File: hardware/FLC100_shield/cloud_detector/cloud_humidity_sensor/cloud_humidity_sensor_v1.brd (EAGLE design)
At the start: 49.5 x 49.5 mm, 21 parts, among them IC1 HIH613x, IC2 HIH612x, IC3 MLX90614, Q1 2N7000, X1 FLC100 SHIELD, X2 MLX90614

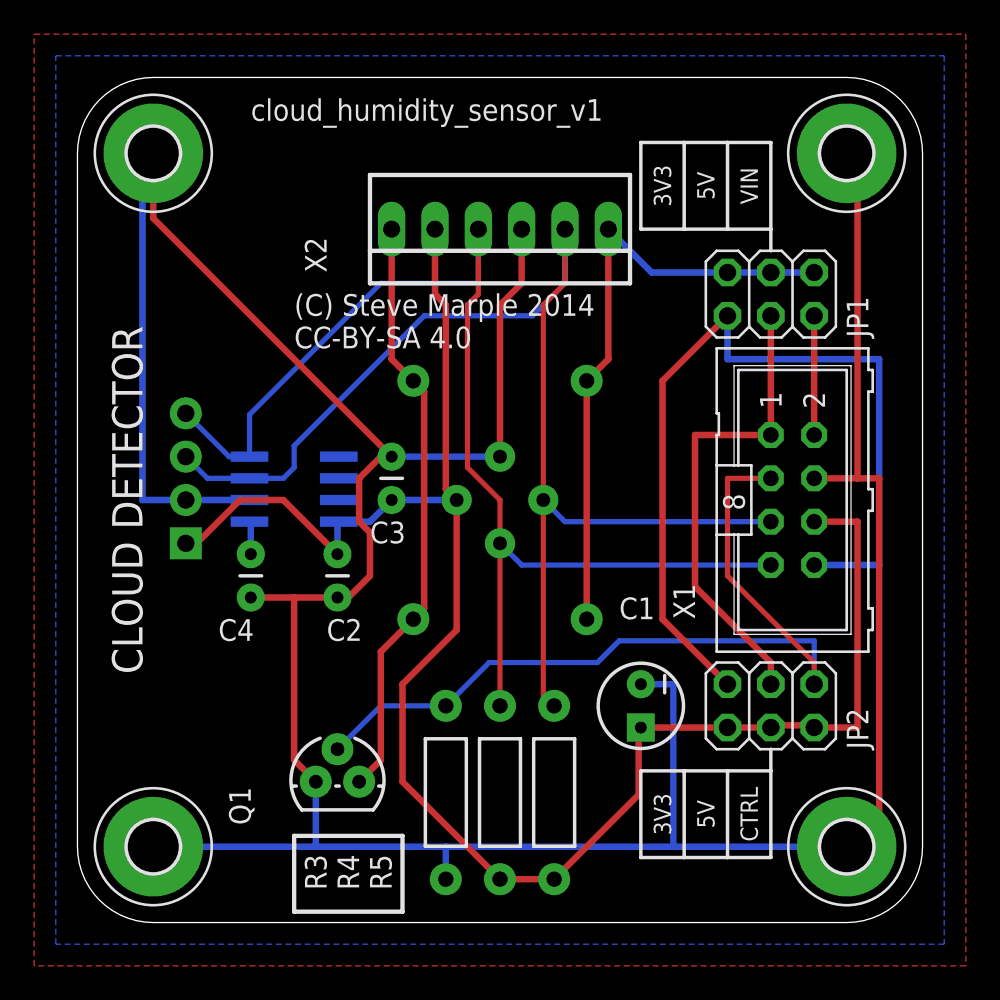
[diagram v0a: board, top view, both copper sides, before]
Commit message: Updating boardd and schematic files to match the Gerber files.
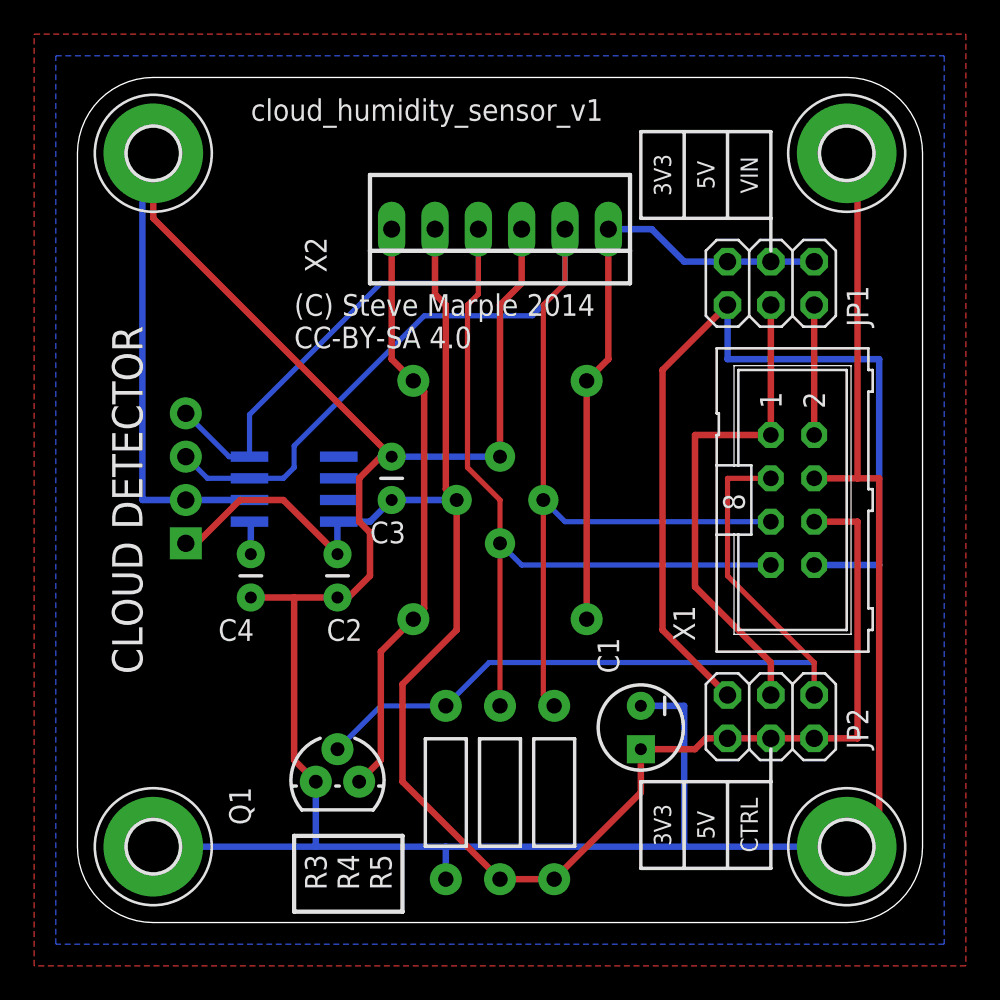
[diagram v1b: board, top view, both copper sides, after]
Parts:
- moved C1 1.27 mm to (33.0, 11.4)
- moved JP1 0.64 mm to (40.6, 37.5)
- moved JP2 0.63 mm to (40.6, 12.1)
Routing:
- net +3V3: track 52.1 -> 54.0 mm
- net +5V: track 27.9 -> 29.1 mm
- net GND: track 201.2 -> 200.5 mm
- net VIN: track 6.99 -> 7.62 mm
- net CONTROL: track 49.8 -> 49.3 mm
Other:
- board text added: ">PLOT_DATE_TIME"
- board text removed: ">LAST_DATE_TIME"
